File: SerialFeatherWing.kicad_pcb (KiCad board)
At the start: 2 copper layers, 50.8 x 22.9 mm, 15 parts, among them J1 feather long, J2 feather short, J3 DB9_Male, U1 ST3232CDR, U2 TC1240AECHTR

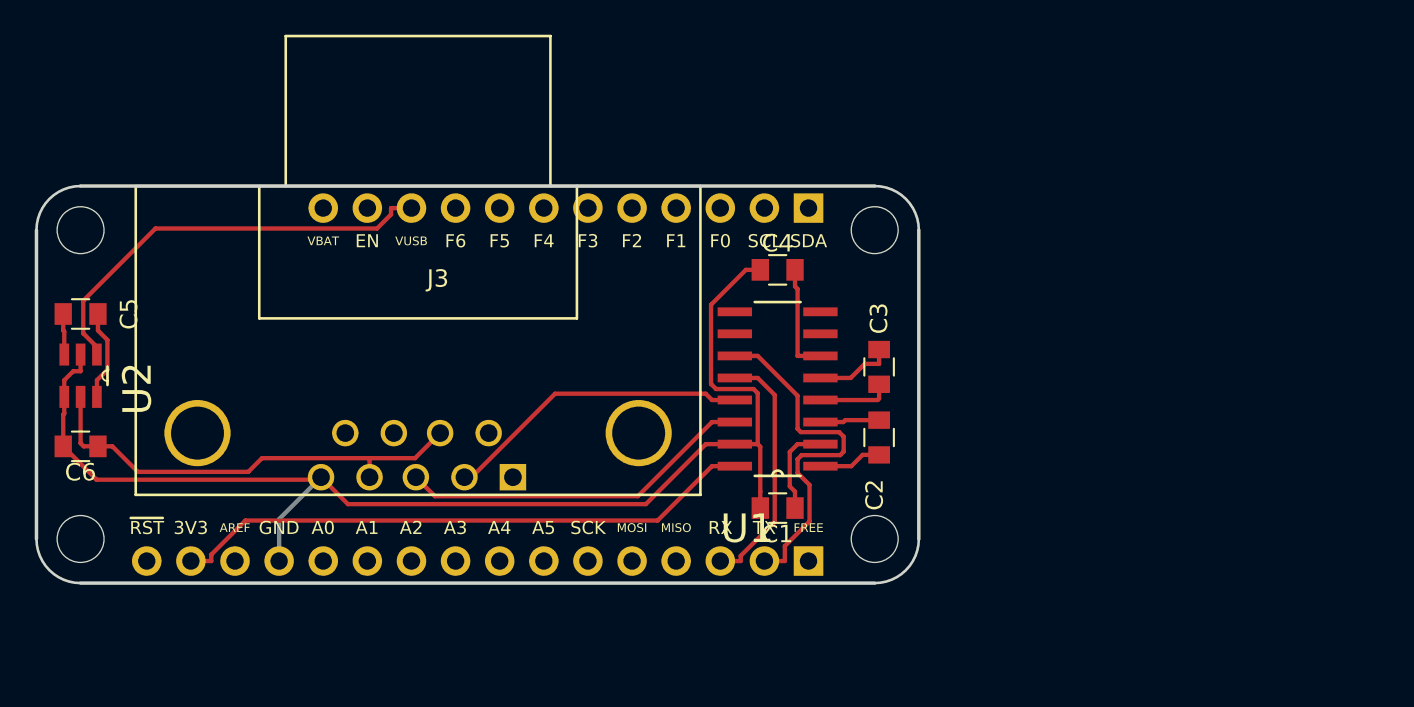
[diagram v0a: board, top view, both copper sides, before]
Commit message: tried connector on end--tested good
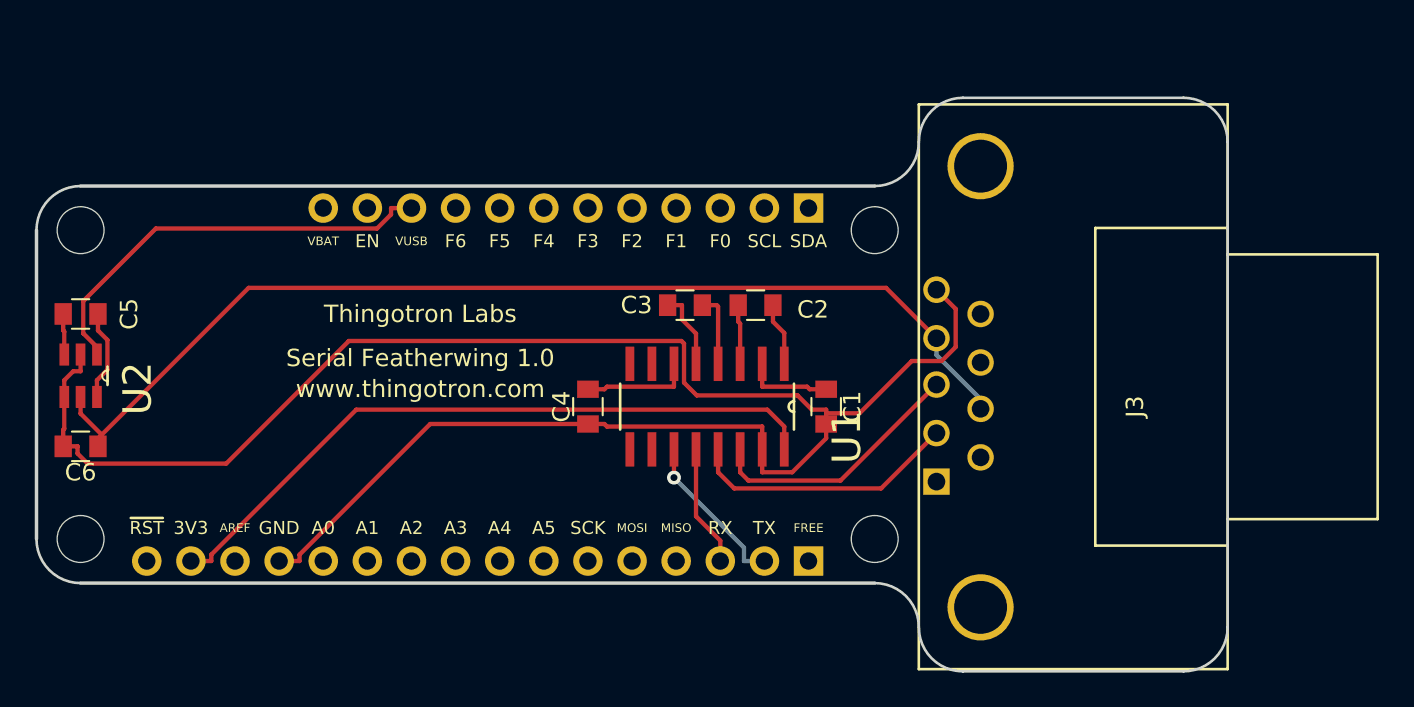
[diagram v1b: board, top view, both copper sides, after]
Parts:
- moved J3 31.5 mm to (78.5, 36.8), turned to 270 degrees
- moved C4 13.5 mm to (57.1, 38.1), turned to 270 degrees
- moved C3 11.7 mm to (62.7, 32.3), turned to 180 degrees
- moved C2 10.4 mm to (66.8, 32.3), turned to 180 degrees
- moved C1 6.48 mm to (70.9, 38.1), turned to 270 degrees
- moved U1 4.19 mm to (64.0, 38.1), turned to 270 degrees
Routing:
- net GND: track 72.5 -> 109.3 mm
- net +10V: track 26.1 -> 61.3 mm
- net TX0: track 20.9 -> 9.27 mm, vias 0 -> 1
- net RX0: track 14.2 -> 7.00 mm
- net +3V3: track 33.8 -> 39.7 mm
- net Net-(J3-Pad3): track 20.6 -> 15.1 mm
- net Net-(J3-Pad2): track 17.7 -> 15.6 mm
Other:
- board size 50.8 x 22.9 mm -> 68.6 x 33 mm
- board text added: "Serial Featherwing 1.0"
- board text added: "Thingotron Labs"
- board text added: "www.thingotron.com"
